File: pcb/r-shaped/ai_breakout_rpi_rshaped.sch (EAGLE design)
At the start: 4 parts

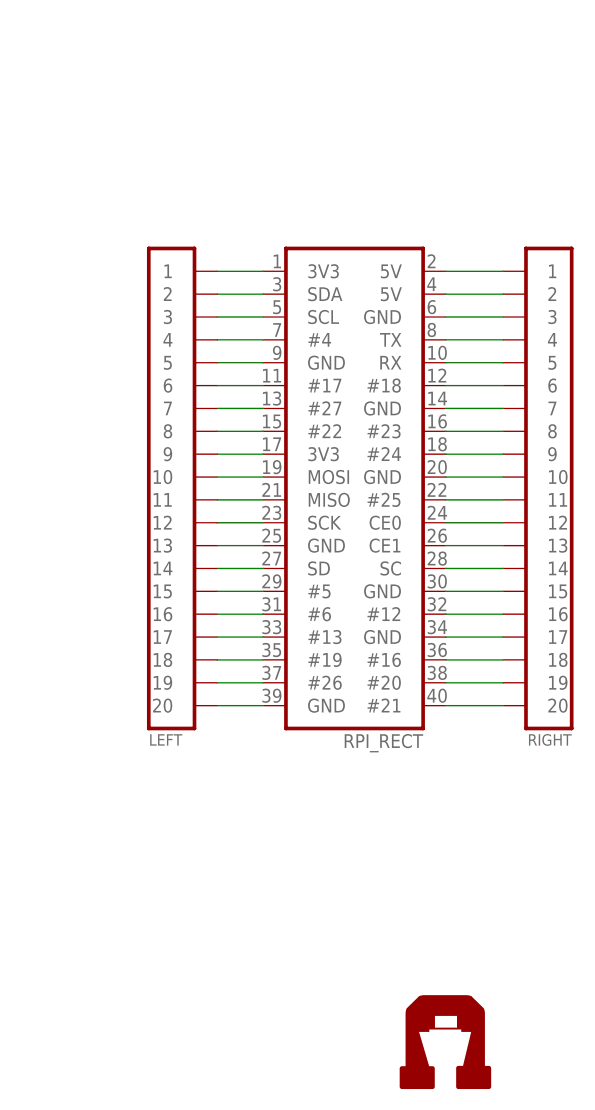
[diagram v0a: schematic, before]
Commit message: Updating T-Shaped.  Added a few labels to R-Shaped
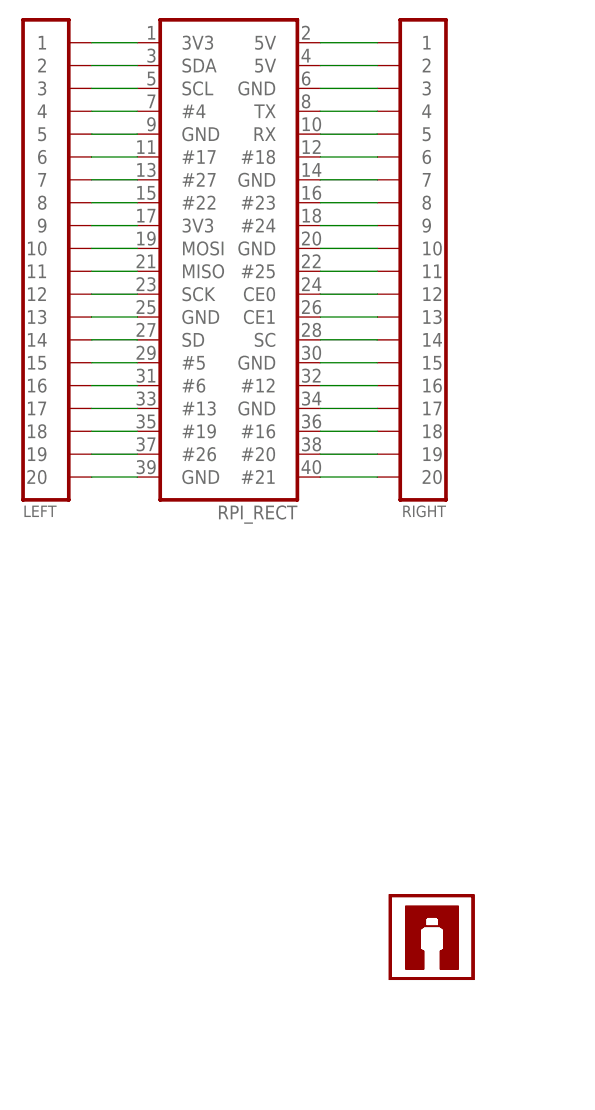
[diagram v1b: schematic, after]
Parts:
- added U$2: AI-LOGOXS, Ai_Miscellany:AI-LOGOXS
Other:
- moved on the sheet: LEFT, RIGHT, RPI_RECT
